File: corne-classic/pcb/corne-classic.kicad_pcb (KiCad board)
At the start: 2 copper layers, 133.8 x 92.2 mm, 98 parts, among them J1 MJ-4PP-9, J2 OLED, J3 LED, P1 i2c-pin, P2 i2c-pin, SW1 SW_PUSH, SW10 SW_PUSH, SW11 SW_PUSH, SW12 SW_PUSH, SW13 SW_PUSH, SW14 SW_PUSH, SW15 SW_PUSH, SW16 SW_PUSH, SW17 SW_PUSH, SW18 SW_PUSH, SW19 SW_PUSH, SW2 SW_PUSH, SW20 SW_PUSH, SW21 SW_PUSH, SW3 SW_PUSH, SW4 SW_PUSH, SW5 SW_PUSH, SW6 SW_PUSH, SW7 SW_PUSH, SW8 SW_PUSH, SW9 SW_PUSH, U1 ProMicro

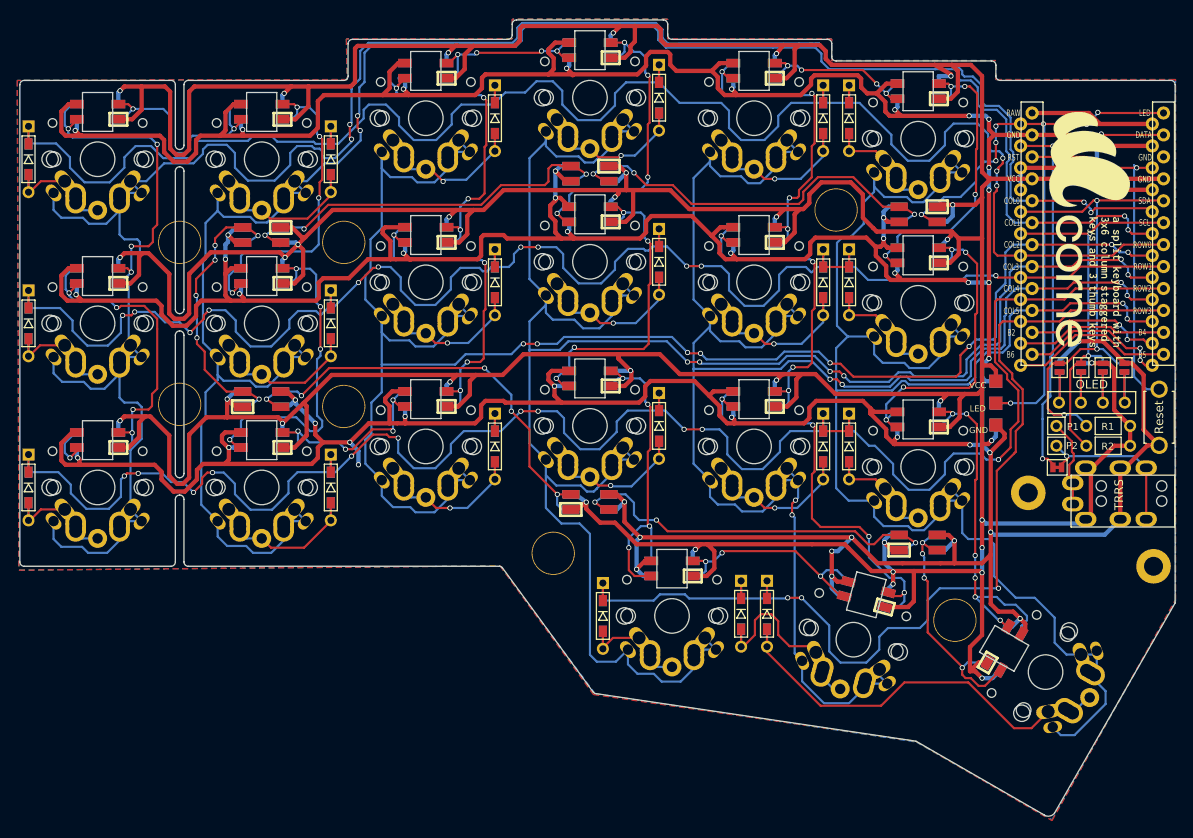
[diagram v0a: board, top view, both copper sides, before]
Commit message: Add a thumb key
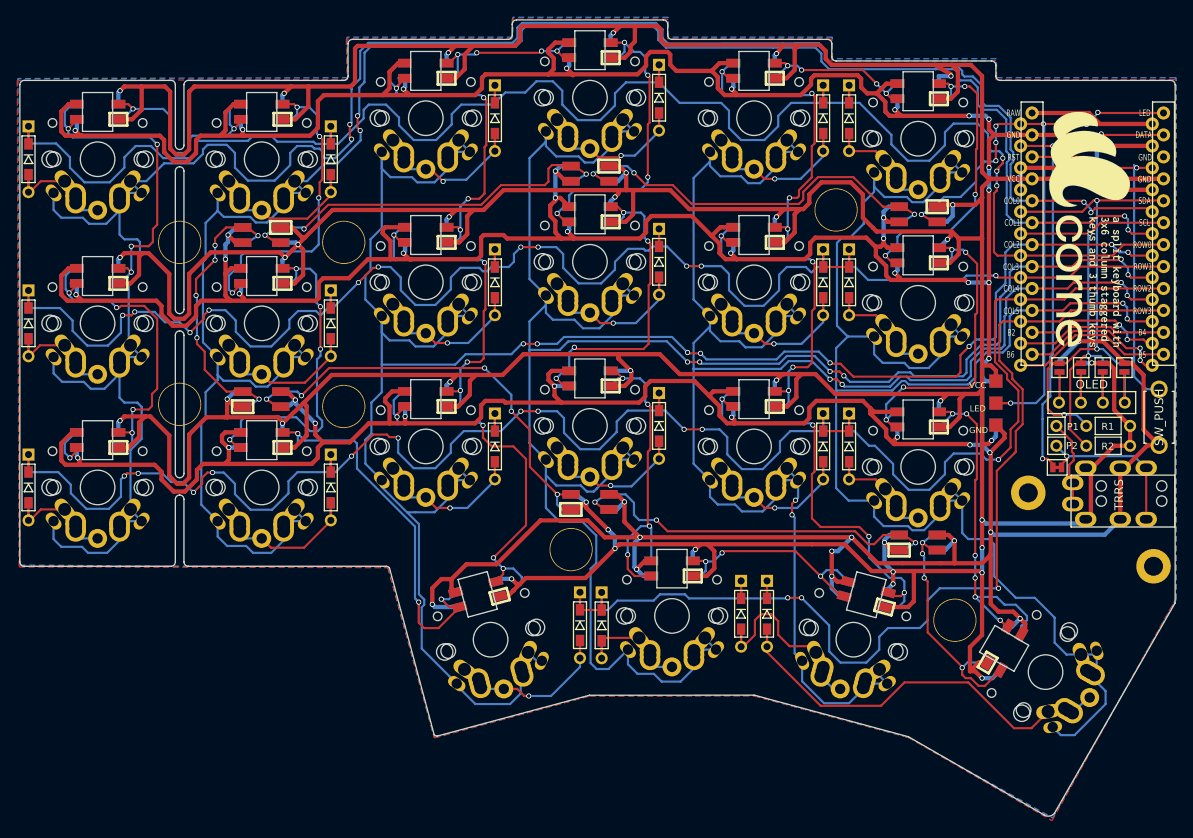
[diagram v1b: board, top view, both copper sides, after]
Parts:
- added D22: D, kbd:D3_TH_SMD, F.Cu at (125.8, 131.1)
- added L28: SK6812MINI, kbd:SK6812MINI_rev, F.Cu at (114.0, 127.5)
- added SW22: SW_PUSH, kbd:MX_ALPS_PG1350_noLed, F.Cu at (115.5, 132.8)
- RSW1: value Reset -> SW_PUSH
- moved ? 2.11 mm to (124.8, 122.3)
- moved D19 1.10 mm to (128.4, 131.1)
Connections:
- L20 pad 3: Net-(L14-Pad3) (its old number) -> Net-(L20-Pad3)
- L21 pad 1: Net-(L14-Pad3) (its old number) -> Net-(L21-Pad1)
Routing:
- net Net-(L21-Pad1): track 0.00 -> 47.5 mm, vias 0 -> 4
- net Net-(L20-Pad3): track 0.00 -> 46.5 mm, vias 0 -> 3
- net col2: track 197.5 -> 237.2 mm
- net GND: track 797.7 -> 829.9 mm, vias 49 -> 48
- net Net-(L14-Pad3) (its old number): track 25.3 -> 0.00 mm, vias 4 -> 0
- net Net-(D22-Pad2): track 0.00 -> 22.0 mm, vias 0 -> 1
- net VCC: track 758.8 -> 778.7 mm, vias 33 -> 36
- net row3: track 121.8 -> 129.0 mm
- net col3: track 225.1 -> 227.1 mm
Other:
- outline, holes or cut-outs redrawn
